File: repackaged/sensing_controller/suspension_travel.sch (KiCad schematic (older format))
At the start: 2 parts

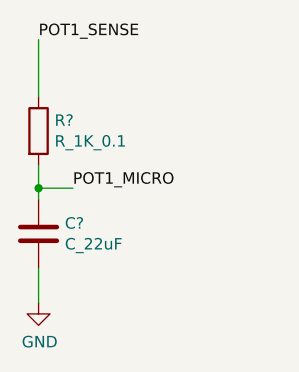
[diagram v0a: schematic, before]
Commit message: Fix net labels, clean schematic.
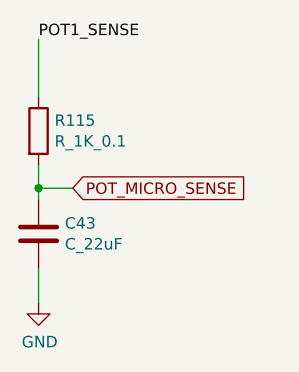
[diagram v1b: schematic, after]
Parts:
- gave numbers to parts that had none: 2
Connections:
- net POT1_MICRO renamed POT_MICRO_SENSE
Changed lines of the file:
@@
 $Descr A4 11693 8268
 encoding utf-8
-Sheet 6 12
+Sheet 18 25
 Title ""
 Date ""
@@
 $EndDescr
 $Comp
-L formula:R_1K_0.1 R?
+L formula:R_1K_0.1 R115
 U 1 1 60A40AD2
 P 5600 3250
-F 0 "R?" H 5670 3296 50  0000 L CNN
+F 0 "R115" H 5670 3296 50  0000 L CNN
 F 1 "R_1K_0.1" H 5670 3205 50  0000 L CNN
 F 2 "footprints:R_0805_OEM" H 5530 3250 50  0001 C CNN
@@
 $EndComp
 $Comp
-L formula:C_22uF C?
+L formula:C_22uF C43
 U 1 1 60A40ADB
 P 5600 3700
-F 0 "C?" H 5715 3746 50  0000 L CNN
+F 0 "C43" H 5715 3746 50  0000 L CNN
 F 1 "C_22uF" H 5715 3655 50  0000 L CNN
 F 2 "footprints:C_1206_OEM" H 5638 3550 50  0001 C CNN
@@
 Text Label 5600 2850 0    50   ~ 0
 POT1_SENSE
-Text Label 5750 3500 0    50   ~ 0
-POT1_MICRO
 Wire Wire Line
 	5600 3850 5600 4000
@@
 	5600 3500 5600 3550
 $Comp
-L power:GND #PWR?
+L power:GND #PWR0186
 U 1 1 60A40AE9
 P 5600 4000
-F 0 "#PWR?" H 5600 3750 50  0001 C CNN
+F 0 "#PWR0186" H 5600 3750 50  0001 C CNN
 F 1 "GND" H 5605 3827 50  0000 C CNN
 F 2 "" H 5600 4000 50  0001 C CNN
@@
 	1    0    0    -1
 $EndComp
+Text GLabel 5750 3500 2    50   Input ~ 0
+POT_MICRO_SENSE
 $EndSCHEMATC

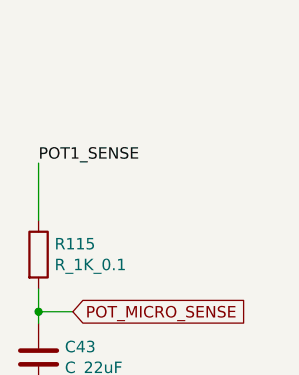
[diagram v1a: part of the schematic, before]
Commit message: Fixed net labels and add missing components.
Changed power flags to global net labels, connected strain gauge nets to ATMEGA16M1, added LEDs where needed, and changed net labels to connect as needed.
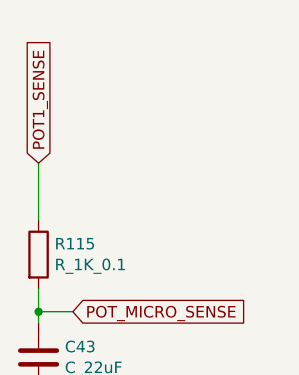
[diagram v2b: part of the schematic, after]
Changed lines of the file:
@@
 Wire Wire Line
 	5600 3400 5600 3500
-Text Label 5600 2850 0    50   ~ 0
-POT1_SENSE
 Wire Wire Line
 	5600 3850 5600 4000
@@
 Text GLabel 5750 3500 2    50   Input ~ 0
 POT_MICRO_SENSE
+Text GLabel 5600 2850 1    50   Input ~ 0
+POT1_SENSE
 $EndSCHEMATC

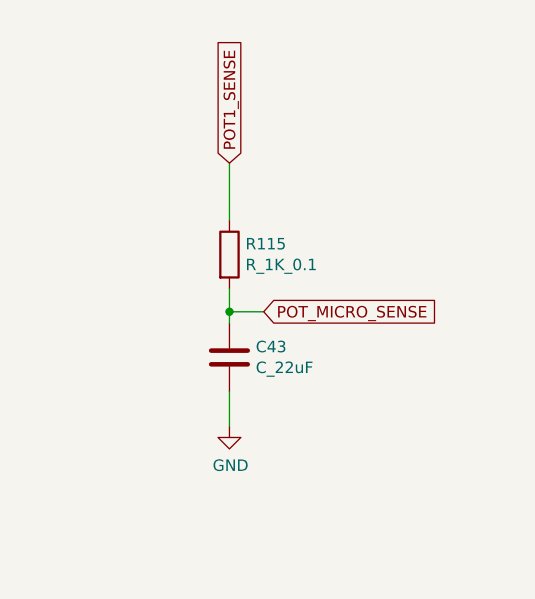
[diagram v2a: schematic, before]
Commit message: moved all circuitry to 50mil grid, fixed net labels, fixed footprints, added connectors
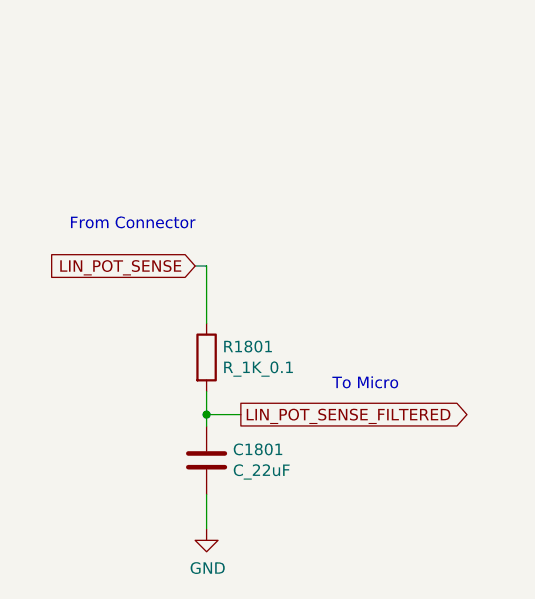
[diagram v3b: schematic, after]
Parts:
- renumbered C43 to C1801, R115 to R1801
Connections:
- net POT1_SENSE renamed LIN_POT_SENSE
- net POT_MICRO_SENSE renamed LIN_POT_SENSE_FILTERED
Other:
- note added: "From Connector"
- note added: "To Micro"
- moved on the sheet: C1801, R1801
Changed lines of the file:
@@
 $Descr A4 11693 8268
 encoding utf-8
-Sheet 18 25
+Sheet 18 20
 Title ""
 Date ""
@@
 $EndDescr
 $Comp
-L formula:R_1K_0.1 R115
+L formula:R_1K_0.1 R1801
 U 1 1 60A40AD2
-P 5600 3250
-F 0 "R115" H 5670 3296 50  0000 L CNN
-F 1 "R_1K_0.1" H 5670 3205 50  0000 L CNN
-F 2 "footprints:R_0805_OEM" H 5530 3250 50  0001 C CNN
-F 3 "https://industrial.panasonic.com/cdbs/www-data/pdf/RDM0000/AOA0000C307.pdf" H 5680 3250 50  0001 C CNN
-F 4 "DK" H 5600 3250 60  0001 C CNN "MFN"
-F 5 "P1.0KDACT-ND" H 5600 3250 60  0001 C CNN "MPN"
-F 6 "https://www.digikey.com/product-detail/en/panasonic-electronic-components/ERA-6AEB102V/P1.0KDACT-ND/1465947" H 6080 3650 60  0001 C CNN "PurchasingLink"
-	1    5600 3250
+P 5500 3700
+F 0 "R1801" H 5570 3746 50  0000 L CNN
+F 1 "R_1K_0.1" H 5570 3655 50  0000 L CNN
+F 2 "footprints:R_0805_OEM" H 5430 3700 50  0001 C CNN
+F 3 "https://industrial.panasonic.com/cdbs/www-data/pdf/RDM0000/AOA0000C307.pdf" H 5580 3700 50  0001 C CNN
+F 4 "DK" H 5500 3700 60  0001 C CNN "MFN"
+F 5 "P1.0KDACT-ND" H 5500 3700 60  0001 C CNN "MPN"
+F 6 "https://www.digikey.com/product-detail/en/panasonic-electronic-components/ERA-6AEB102V/P1.0KDACT-ND/1465947" H 5980 4100 60  0001 C CNN "PurchasingLink"
+	1    5500 3700
 	1    0    0    -1
 $EndComp
 $Comp
-L formula:C_22uF C43
+L formula:C_22uF C1801
 U 1 1 60A40ADB
-P 5600 3700
-F 0 "C43" H 5715 3746 50  0000 L CNN
-F 1 "C_22uF" H 5715 3655 50  0000 L CNN
-F 2 "footprints:C_1206_OEM" H 5638 3550 50  0001 C CNN
-F 3 "https://product.tdk.com/info/en/catalog/datasheets/mlcc_commercial_general_en.pdf" H 5625 3800 50  0001 C CNN
-F 4 "DK" H 5600 3700 60  0001 C CNN "MFN"
-F 5 "445-11693-1-ND" H 5600 3700 60  0001 C CNN "MPN"
-F 6 "https://www.digikey.com/product-detail/en/tdk-corporation/C3216JB1C226M160AB/445-11693-1-ND/3953359" H 6025 4200 60  0001 C CNN "PurchasingLink"
-	1    5600 3700
+P 5500 4150
+F 0 "C1801" H 5615 4196 50  0000 L CNN
+F 1 "C_22uF" H 5615 4105 50  0000 L CNN
+F 2 "footprints:C_1206_OEM" H 5538 4000 50  0001 C CNN
+F 3 "https://product.tdk.com/info/en/catalog/datasheets/mlcc_commercial_general_en.pdf" H 5525 4250 50  0001 C CNN
+F 4 "DK" H 5500 4150 60  0001 C CNN "MFN"
+F 5 "445-11693-1-ND" H 5500 4150 60  0001 C CNN "MPN"
+F 6 "https://www.digikey.com/product-detail/en/tdk-corporation/C3216JB1C226M160AB/445-11693-1-ND/3953359" H 5925 4650 60  0001 C CNN "PurchasingLink"
+	1    5500 4150
 	1    0    0    -1
 $EndComp
 Wire Wire Line
-	5600 3400 5600 3500
+	5500 3850 5500 3950
 Wire Wire Line
-	5600 3850 5600 4000
+	5500 4300 5500 4450
 Wire Wire Line
-	5600 3100 5600 2850
+	5500 3550 5500 3300
 Wire Wire Line
-	5600 3500 5750 3500
-Connection ~ 5600 3500
+	5500 3950 5650 3950
+Connection ~ 5500 3950
 Wire Wire Line
-	5600 3500 5600 3550
+	5500 3950 5500 4000
 $Comp
-L power:GND #PWR0186
+L power:GND #PWR01801
 U 1 1 60A40AE9
-P 5600 4000
-F 0 "#PWR0186" H 5600 3750 50  0001 C CNN
-F 1 "GND" H 5605 3827 50  0000 C CNN
-F 2 "" H 5600 4000 50  0001 C CNN
-F 3 "" H 5600 4000 50  0001 C CNN
-	1    5600 4000
+P 5500 4450
+F 0 "#PWR01801" H 5500 4200 50  0001 C CNN
+F 1 "GND" H 5505 4277 50  0000 C CNN
+F 2 "" H 5500 4450 50  0001 C CNN
+F 3 "" H 5500 4450 50  0001 C CNN
+	1    5500 4450
 	1    0    0    -1
 $EndComp
-Text GLabel 5750 3500 2    50   Input ~ 0
-POT_MICRO_SENSE
-Text GLabel 5600 2850 1    50   Input ~ 0
-POT1_SENSE
+Text GLabel 5650 3950 2    50   Output ~ 0
+LIN_POT_SENSE_FILTERED
+Wire Wire Line
+	5450 3300 5500 3300
+Text Notes 4900 3150 0    50   ~ 0
+From Connector
+Text Notes 6050 3850 0    50   ~ 0
+To Micro
+Text GLabel 5450 3300 0    50   Input ~ 0
+LIN_POT_SENSE
 $EndSCHEMATC
